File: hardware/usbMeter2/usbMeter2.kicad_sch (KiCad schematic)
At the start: 27 parts, among them J1 USB_A, J2 USB_A, J3 USB_C_Receptacle_USB2.0_16P, SW1 SW_Push, SW2 SW_Push, SW3 SW_Push, U1 STM32G031G8Ux, U2 TPD4E05U06DQA, U3 TPD4E05U06DQA, U4 CH340E

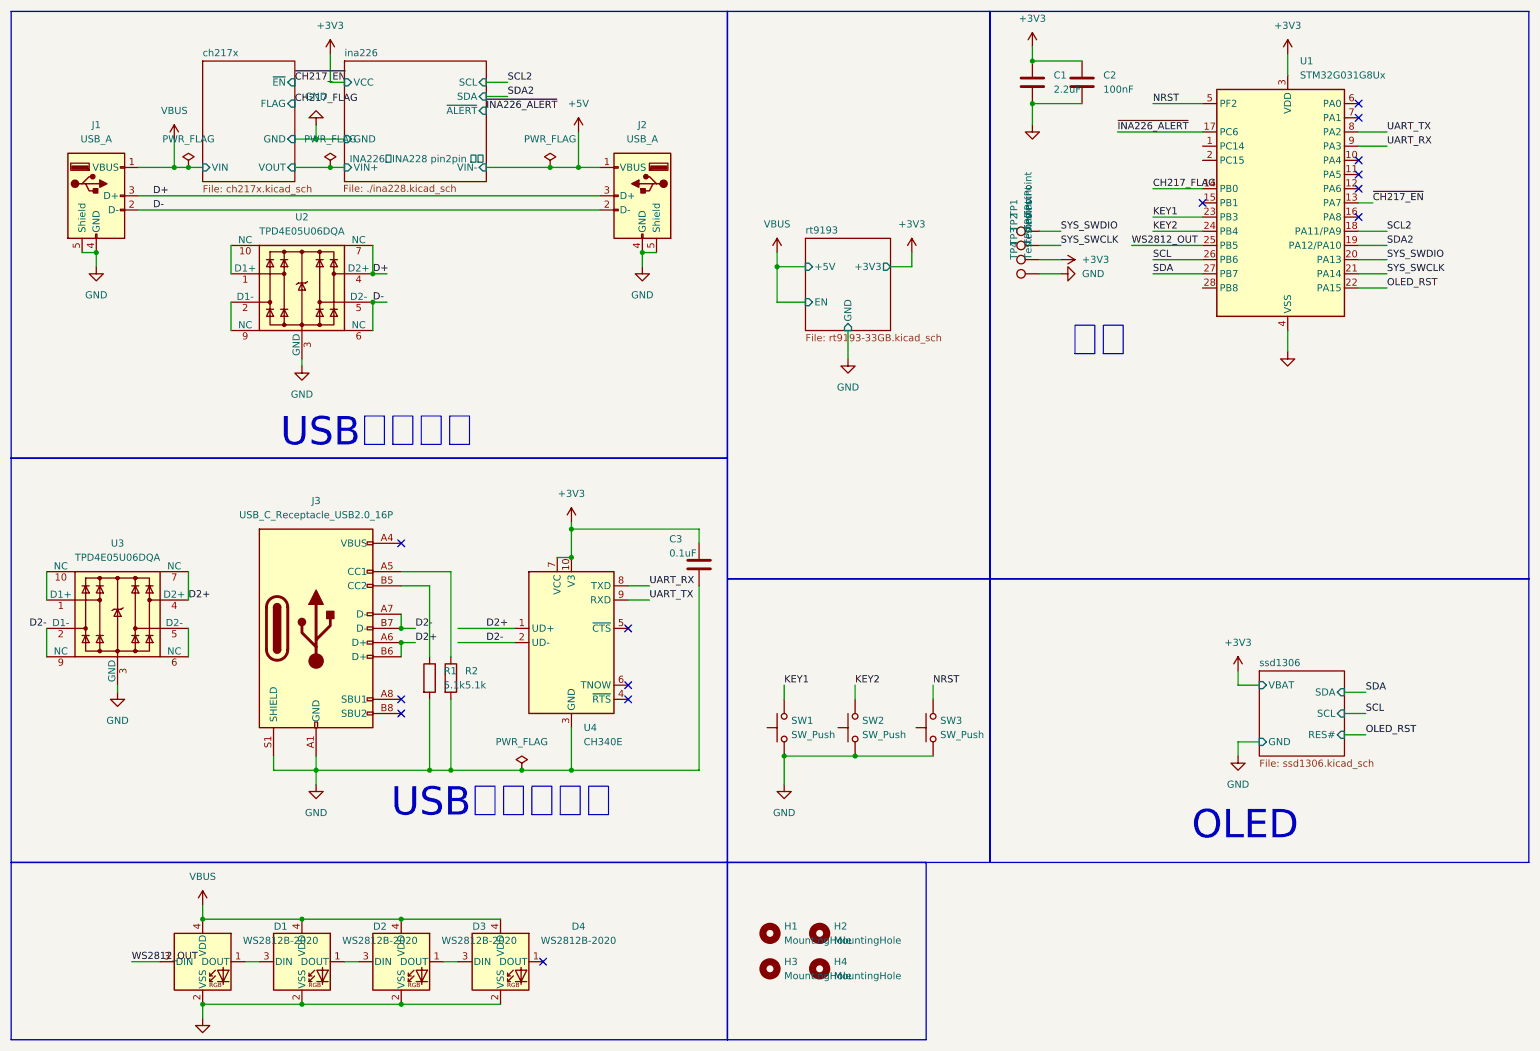
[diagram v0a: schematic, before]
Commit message: usbmeter2尝试缩减了本体的尺寸，采用dcdc+ldo供电避免typea可能存在的高压输入
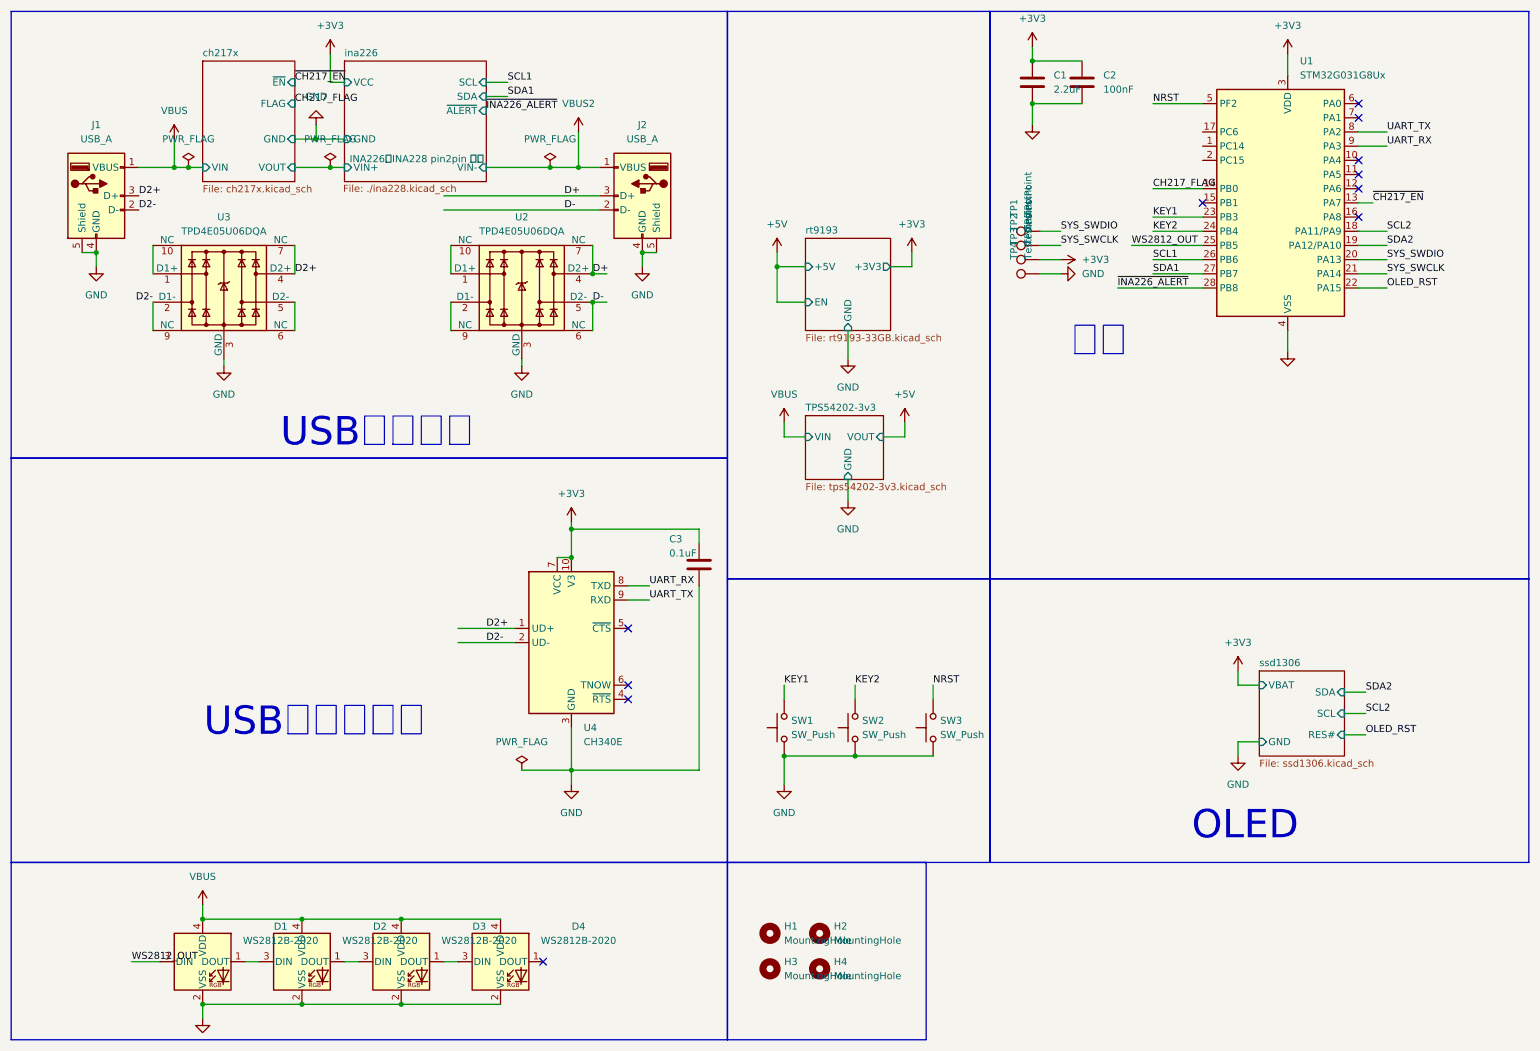
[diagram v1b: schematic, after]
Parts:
- removed J3: USB_C_Receptacle_USB2.0_16P, Connector_USB:USB_C_Receptacle_GCT_USB4105-xx-A_16P_TopMnt_Horizontal, symbol Connector:USB_C_Receptacle_USB2.0_16P
- removed R1, R2: 5.1k, Resistor_SMD:R_0402_1005Metric, symbol Device:R
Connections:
- net +5V: no longer J2.1 (VBUS)
- net D+: no longer J1.3 (D+)
- net D-: no longer J1.2 (D-)
- net D2+: now also J1.3 (D+)
- net D2-: now also J1.2 (D-)
- net ~{INA226_ALERT}: now also U1.28 (PB8); no longer U1.17 (PC6)
- net SCL renamed SCL1
- net SDA renamed SDA1
- new net VBUS2: J2.1 (VBUS)
- no-connect marks 14 -> 11
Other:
- added sheet TPS54202-3v3 (tps54202-3v3.kicad_sch)
- moved on the sheet: U2, U3
